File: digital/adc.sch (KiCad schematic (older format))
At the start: 1 part

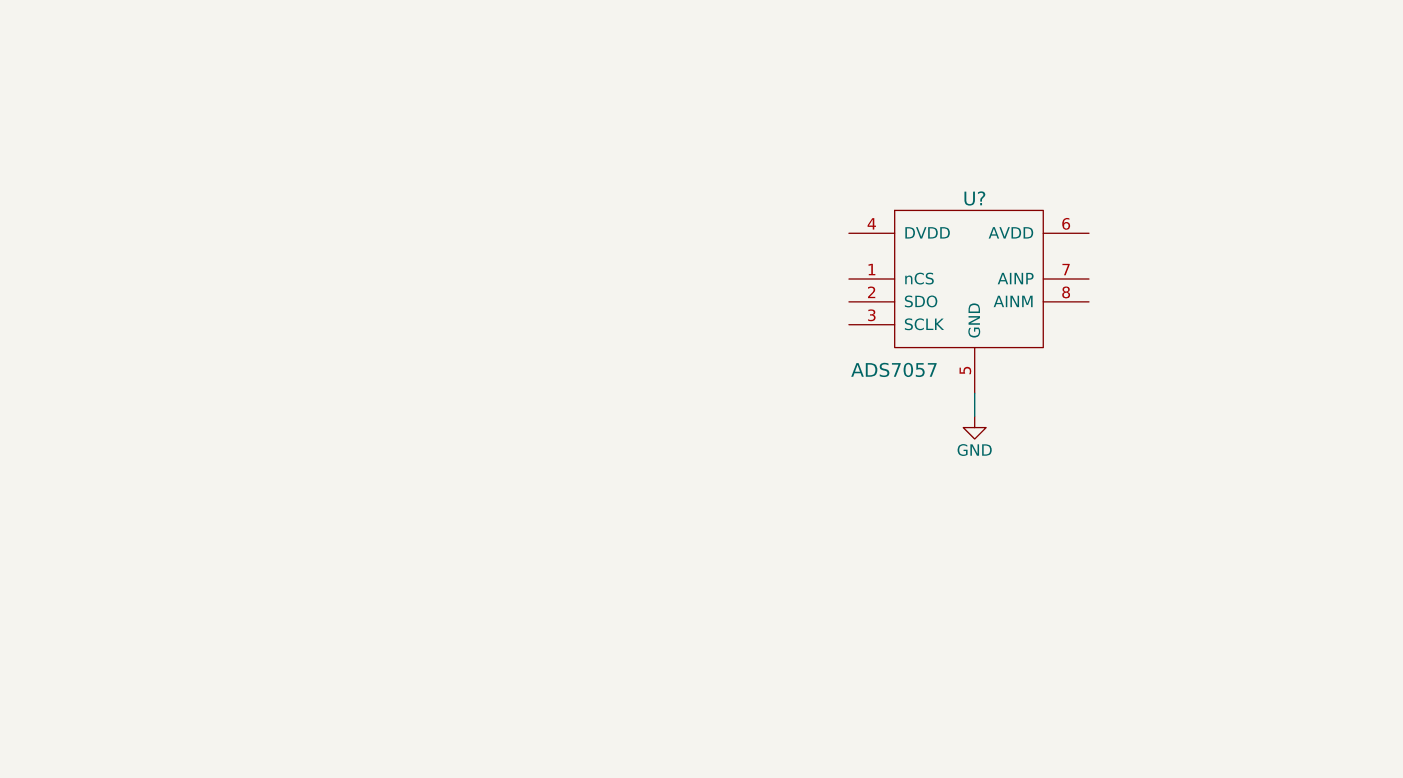
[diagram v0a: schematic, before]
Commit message: Finish schematic TODO footprints
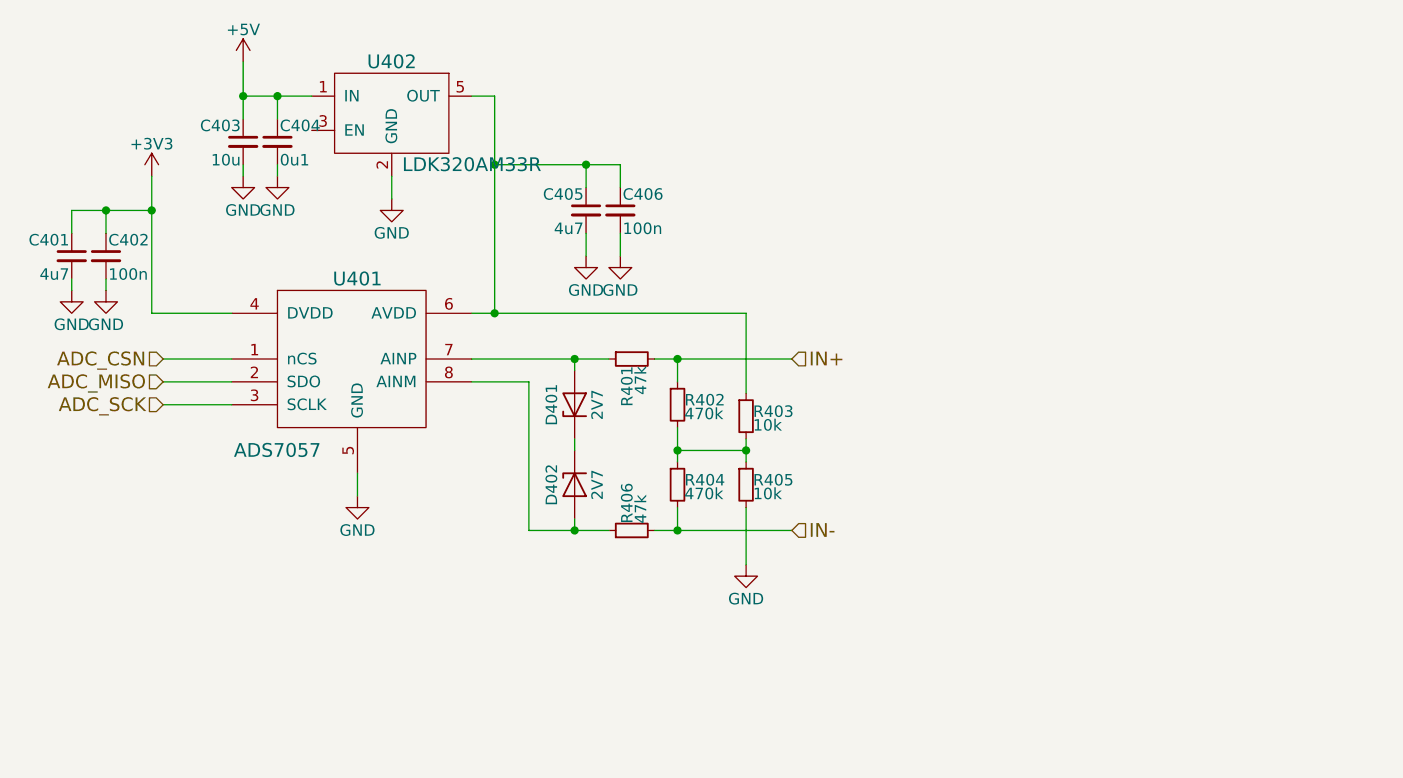
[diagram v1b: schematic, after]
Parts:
- added C401, C405: 4u7, symbol C_Small
- added C402, C406: 100n, symbol C_Small
- added C403: 10u, symbol C_Small
- added C404: 0u1, symbol C_Small
- added D401, D402: 2V7, symbol D_Zener
- added R401, R406: 47k, symbol R_Small
- added R402, R404: 470k, symbol R_Small
- added R403, R405: 10k, symbol R_Small
- added U402: LDK320AM33R, symbol LDK320AM33R
- gave numbers to parts that had none: 1
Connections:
- net GND: now also C401.2, C402.2, C403.2, C404.2, C405.2, C406.2, R405.2, U402.2 (GND)
- net ADC_CSN: now reaches U401.1 (nCS)
- net ADC_MISO: now reaches U401.2 (SDO)
- net ADC_SCK: now reaches U401.3 (SCLK)
- net +3V3: now reaches U401.4 (DVDD)
- net +3V3: now also C401.1, C402.1
- net at U401.6 (AVDD): now also C405.1, C406.1, R403.1, U402.5 (OUT)
- net at U401.7 (AINP): now also D401.2 (A), R401.1
- net at U401.8 (AINM): now also D402.2 (A), R406.1
- new net: D401.1 (K), D402.1 (K)
- new net: R402.2, R403.2, R404.1, R405.1
- new net +5V: C403.1, C404.1, U402.1 (IN)
- new net IN+: R401.2, R402.1
- new net IN-: R404.2, R406.2
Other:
- moved on the sheet: U401

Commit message: Finish schematic and footprinting of digital board
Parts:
- C401, C405: footprint (none) -> Capacitors_SMD:C_1206_HandSoldering
- C402, C404, C406: footprint (none) -> Capacitors_SMD:C_0603_HandSoldering
- C403: footprint (none) -> Capacitors_SMD:C_0805_HandSoldering
- D401, D402: footprint (none) -> Diodes_SMD:D_SOD-323_HandSoldering
- R401, R403, R405, R406: footprint (none) -> Resistors_SMD:R_0603_HandSoldering
- R402, R404: footprint (none) -> Resistors_SMD:R_0402
- U401: footprint (none) -> digital:TI_X2QFN8
- U402: footprint (none) -> digital:ST_SOT23-5L
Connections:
- no-connect marks 0 -> 1
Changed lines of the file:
@@
 F 0 "U401" H 4950 3950 60  0000 C CNN
 F 1 "ADS7057" H 4600 3200 60  0000 C CNN
-F 2 "" H 4950 3650 60  0001 C CNN
+F 2 "digital:TI_X2QFN8" H 4950 3650 60  0001 C CNN
 F 3 "https://www.mouser.com/ProductDetail/Texas-Instruments/ADS7054IRUGR?qs=sGAEpiMZZMvTvDTV69d2QmaaDF3oWAC7QmNCEdeiHEg%3d" H 4950 3650 60  0001 C CNN
 	1    4950 3650
@@
 $EndComp
 $Comp
-L GND #PWR410
+L GND #PWR087
 U 1 1 5AD34755
 P 4950 4300
-F 0 "#PWR410" H 4950 4050 50  0001 C CNN
+F 0 "#PWR087" H 4950 4050 50  0001 C CNN
 F 1 "GND" H 4950 4150 50  0000 C CNN
 F 2 "" H 4950 4300 50  0001 C CNN
@@
 ADC_SCK
 $Comp
-L +3V3 #PWR402
+L +3V3 #PWR088
 U 1 1 5AD705AE
 P 4050 2900
-F 0 "#PWR402" H 4050 2750 50  0001 C CNN
+F 0 "#PWR088" H 4050 2750 50  0001 C CNN
 F 1 "+3V3" H 4050 3040 50  0000 C CNN
 F 2 "" H 4050 2900 50  0001 C CNN
@@
 F 0 "C402" H 3860 3320 50  0000 L CNN
 F 1 "100n" H 3860 3170 50  0000 L CNN
-F 2 "" H 3850 3250 50  0001 C CNN
+F 2 "Capacitors_SMD:C_0603_HandSoldering" H 3850 3250 50  0001 C CNN
 F 3 "" H 3850 3250 50  0001 C CNN
 	1    3850 3250
@@
 F 0 "C401" H 3710 3320 50  0000 L CNN
 F 1 "4u7" H 3710 3170 50  0000 L CNN
-F 2 "" H 3700 3250 50  0001 C CNN
+F 2 "Capacitors_SMD:C_1206_HandSoldering" H 3700 3250 50  0001 C CNN
 F 3 "" H 3700 3250 50  0001 C CNN
 	1    3700 3250
@@
 $EndComp
 $Comp
-L GND #PWR409
+L GND #PWR089
 U 1 1 5AD7062F
 P 3850 3400
-F 0 "#PWR409" H 3850 3150 50  0001 C CNN
+F 0 "#PWR089" H 3850 3150 50  0001 C CNN
 F 1 "GND" H 3850 3250 50  0000 C CNN
 F 2 "" H 3850 3400 50  0001 C CNN
@@
 $EndComp
 $Comp
-L GND #PWR408
+L GND #PWR090
 U 1 1 5AD7064A
 P 3700 3400
-F 0 "#PWR408" H 3700 3150 50  0001 C CNN
+F 0 "#PWR090" H 3700 3150 50  0001 C CNN
 F 1 "GND" H 3700 3250 50  0000 C CNN
 F 2 "" H 3700 3400 50  0001 C CNN
@@
 F 0 "D402" H 5900 4350 50  0000 C CNN
 F 1 "2V7" H 5900 4150 50  0000 C CNN
-F 2 "" H 5900 4250 50  0001 C CNN
+F 2 "Diodes_SMD:D_SOD-323_HandSoldering" H 5900 4250 50  0001 C CNN
 F 3 "https://www.mouser.com/ProductDetail/ON-Semiconductor/MM3Z2V7ST1G?qs=sGAEpiMZZMtQ8nqTKtFS%2fJ7m6e1KBCguKFeJwHBR4ZU%3d" H 5900 4250 50  0001 C CNN
 	1    5900 4250
@@
 F 0 "D401" H 5900 4000 50  0000 C CNN
 F 1 "2V7" H 5900 3800 50  0000 C CNN
-F 2 "" H 5900 3900 50  0001 C CNN
+F 2 "Diodes_SMD:D_SOD-323_HandSoldering" H 5900 3900 50  0001 C CNN
 F 3 "https://www.mouser.com/ProductDetail/ON-Semiconductor/MM3Z2V7ST1G?qs=sGAEpiMZZMtQ8nqTKtFS%2fJ7m6e1KBCguKFeJwHBR4ZU%3d" H 5900 3900 50  0001 C CNN
 	1    5900 3900
@@
 F 0 "R401" H 6180 3720 50  0000 L CNN
 F 1 "47k" H 6180 3660 50  0000 L CNN
-F 2 "" H 6150 3700 50  0001 C CNN
+F 2 "Resistors_SMD:R_0603_HandSoldering" H 6150 3700 50  0001 C CNN
 F 3 "" H 6150 3700 50  0001 C CNN
 	1    6150 3700
@@
 F 0 "R406" H 6180 4470 50  0000 L CNN
 F 1 "47k" H 6180 4410 50  0000 L CNN
-F 2 "" H 6150 4450 50  0001 C CNN
+F 2 "Resistors_SMD:R_0603_HandSoldering" H 6150 4450 50  0001 C CNN
 F 3 "" H 6150 4450 50  0001 C CNN
 	1    6150 4450
@@
 F 0 "R402" H 6380 3920 50  0000 L CNN
 F 1 "470k" H 6380 3860 50  0000 L CNN
-F 2 "" H 6350 3900 50  0001 C CNN
+F 2 "Resistors_SMD:R_0402" H 6350 3900 50  0001 C CNN
 F 3 "" H 6350 3900 50  0001 C CNN
 	1    6350 3900
@@
 F 0 "R404" H 6380 4270 50  0000 L CNN
 F 1 "470k" H 6380 4210 50  0000 L CNN
-F 2 "" H 6350 4250 50  0001 C CNN
+F 2 "Resistors_SMD:R_0402" H 6350 4250 50  0001 C CNN
 F 3 "" H 6350 4250 50  0001 C CNN
 	1    6350 4250
@@
 F 0 "R403" H 6680 3970 50  0000 L CNN
 F 1 "10k" H 6680 3910 50  0000 L CNN
-F 2 "" H 6650 3950 50  0001 C CNN
+F 2 "Resistors_SMD:R_0603_HandSoldering" H 6650 3950 50  0001 C CNN
 F 3 "" H 6650 3950 50  0001 C CNN
 	1    6650 3950
@@
 F 0 "R405" H 6680 4270 50  0000 L CNN
 F 1 "10k" H 6680 4210 50  0000 L CNN
-F 2 "" H 6650 4250 50  0001 C CNN
+F 2 "Resistors_SMD:R_0603_HandSoldering" H 6650 4250 50  0001 C CNN
 F 3 "" H 6650 4250 50  0001 C CNN
 	1    6650 4250
@@
 Connection ~ 6350 4100
 $Comp
-L GND #PWR411
+L GND #PWR091
 U 1 1 5AD86212
 P 6650 4600
-F 0 "#PWR411" H 6650 4350 50  0001 C CNN
+F 0 "#PWR091" H 6650 4350 50  0001 C CNN
 F 1 "GND" H 6650 4450 50  0000 C CNN
 F 2 "" H 6650 4600 50  0001 C CNN
@@
 F 0 "C406" H 6110 3120 50  0000 L CNN
 F 1 "100n" H 6110 2970 50  0000 L CNN
-F 2 "" H 6100 3050 50  0001 C CNN
+F 2 "Capacitors_SMD:C_0603_HandSoldering" H 6100 3050 50  0001 C CNN
 F 3 "" H 6100 3050 50  0001 C CNN
 	1    6100 3050
@@
 F 0 "C405" H 5960 3120 50  0000 L CNN
 F 1 "4u7" H 5960 2970 50  0000 L CNN
-F 2 "" H 5950 3050 50  0001 C CNN
+F 2 "Capacitors_SMD:C_1206_HandSoldering" H 5950 3050 50  0001 C CNN
 F 3 "" H 5950 3050 50  0001 C CNN
 	1    5950 3050
@@
 $EndComp
 $Comp
-L GND #PWR406
+L GND #PWR092
 U 1 1 5AD86984
 P 5950 3250
-F 0 "#PWR406" H 5950 3000 50  0001 C CNN
+F 0 "#PWR092" H 5950 3000 50  0001 C CNN
 F 1 "GND" H 5950 3100 50  0000 C CNN
 F 2 "" H 5950 3250 50  0001 C CNN
@@
 $EndComp
 $Comp
-L GND #PWR407
+L GND #PWR093
 U 1 1 5AD869BD
 P 6100 3250
-F 0 "#PWR407" H 6100 3000 50  0001 C CNN
+F 0 "#PWR093" H 6100 3000 50  0001 C CNN
 F 1 "GND" H 6100 3100 50  0000 C CNN
 F 2 "" H 6100 3250 50  0001 C CNN
@@
 U 1 1 5ADA8C95
 P 5100 2550
+AR Path="/5ADA8C95" Ref="U402"  Part="1"
+AR Path="/5AD346DB/5ADA8C95" Ref="U402"  Part="1"
 F 0 "U402" H 5100 2700 60  0000 C CNN
 F 1 "LDK320AM33R" H 5450 2250 60  0000 C CNN
-F 2 "" H 5100 2550 60  0001 C CNN
+F 2 "digital:ST_SOT23-5L" H 5100 2550 60  0001 C CNN
 F 3 "https://www.mouser.com/ProductDetail/STMicroelectronics/LDK320AM33R?qs=sGAEpiMZZMsGz1a6aV8DcGP3s75Ab7uy0gVNUtcA%252bWU%3d" H 5100 2550 60  0001 C CNN
 	1    5100 2550
@@
 Connection ~ 5550 2850
 $Comp
-L +5V #PWR401
+L +5V #PWR094
 U 1 1 5ADA8E18
 P 4450 2400
-F 0 "#PWR401" H 4450 2250 50  0001 C CNN
+F 0 "#PWR094" H 4450 2250 50  0001 C CNN
 F 1 "+5V" H 4450 2540 50  0000 C CNN
 F 2 "" H 4450 2400 50  0001 C CNN
@@
 F 0 "C404" H 4610 2820 50  0000 L CNN
 F 1 "0u1" H 4610 2670 50  0000 L CNN
-F 2 "" H 4600 2750 50  0001 C CNN
+F 2 "Capacitors_SMD:C_0603_HandSoldering" H 4600 2750 50  0001 C CNN
 F 3 "" H 4600 2750 50  0001 C CNN
 	1    4600 2750
@@
 F 0 "C403" H 4460 2820 50  0000 L CNN
 F 1 "10u" H 4460 2670 50  0000 L CNN
-F 2 "" H 4450 2750 50  0001 C CNN
+F 2 "Capacitors_SMD:C_0805_HandSoldering" H 4450 2750 50  0001 C CNN
 F 3 "" H 4450 2750 50  0001 C CNN
 	1    4450 2750
@@
 $EndComp
 $Comp
-L GND #PWR403
+L GND #PWR095
 U 1 1 5ADA8EE6
 P 4450 2900
-F 0 "#PWR403" H 4450 2650 50  0001 C CNN
+F 0 "#PWR095" H 4450 2650 50  0001 C CNN
 F 1 "GND" H 4450 2750 50  0000 C CNN
 F 2 "" H 4450 2900 50  0001 C CNN
@@
 	4450 2850 4450 2900
 $Comp
-L GND #PWR404
+L GND #PWR096
 U 1 1 5ADA8FD8
 P 4600 2900
-F 0 "#PWR404" H 4600 2650 50  0001 C CNN
+F 0 "#PWR096" H 4600 2650 50  0001 C CNN
 F 1 "GND" H 4600 2750 50  0000 C CNN
 F 2 "" H 4600 2900 50  0001 C CNN
@@
 Connection ~ 4600 2550
 $Comp
-L GND #PWR405
+L GND #PWR097
 U 1 1 5ADA9622
 P 5100 3000
-F 0 "#PWR405" H 5100 2750 50  0001 C CNN
+F 0 "#PWR097" H 5100 2750 50  0001 C CNN
 F 1 "GND" H 5100 2850 50  0000 C CNN
 F 2 "" H 5100 3000 50  0001 C CNN
@@
 Wire Wire Line
 	5100 2900 5100 3000
+NoConn ~ 4750 2700
 $EndSCHEMATC

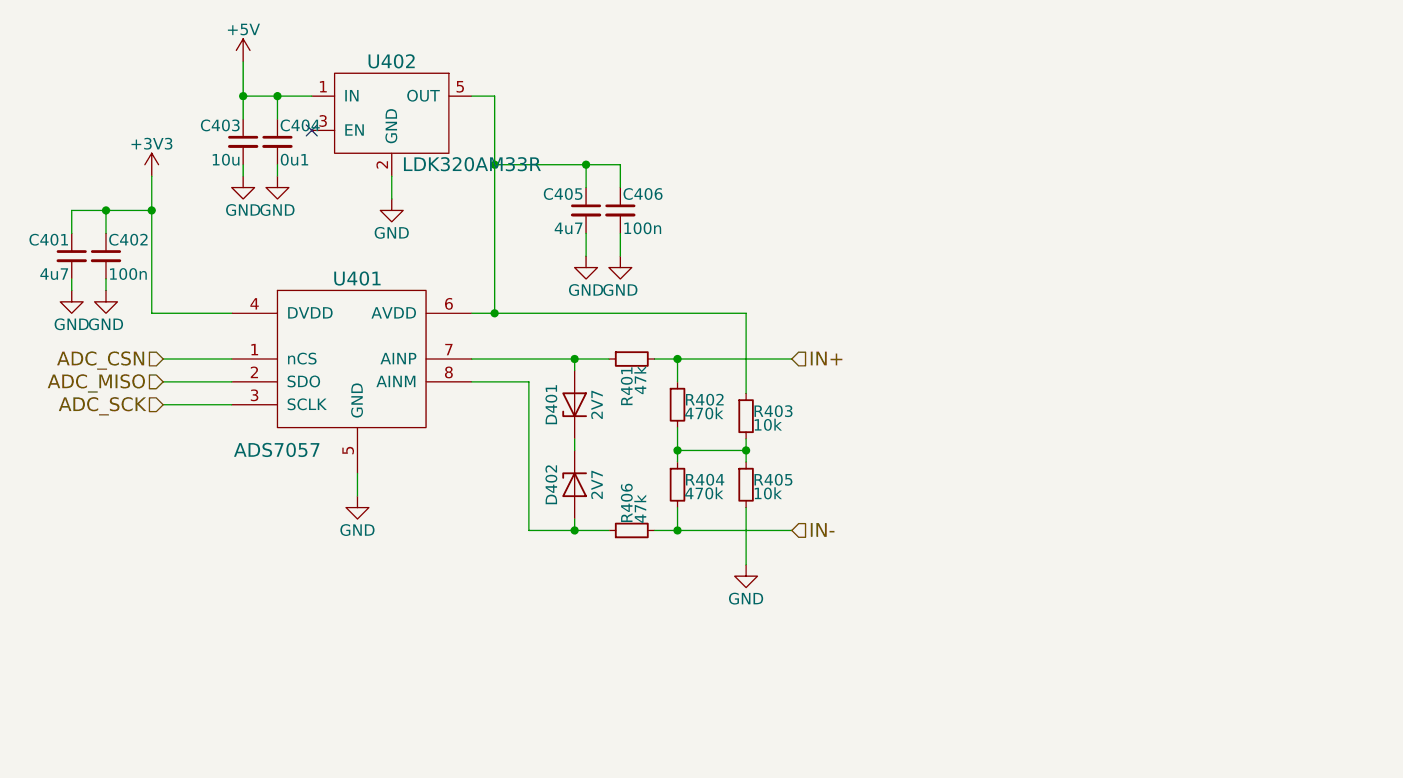
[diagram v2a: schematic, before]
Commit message: Add gain stage; hopefully ready to start layout now
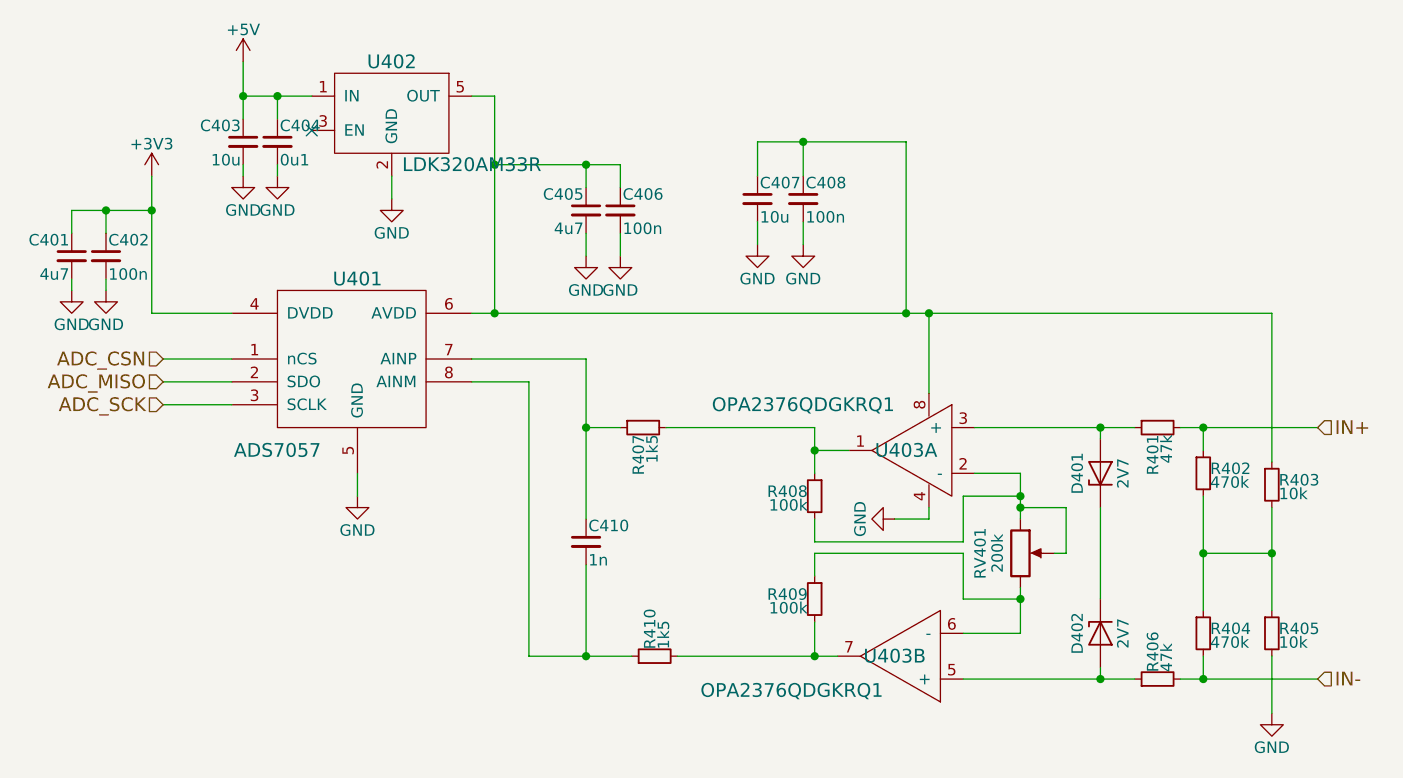
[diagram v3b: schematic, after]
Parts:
- added C407: 10u, Capacitors_SMD:C_0805_HandSoldering, symbol C_Small
- added C408: 100n, Capacitors_SMD:C_0603_HandSoldering, symbol C_Small
- added C410: 1n, Capacitors_SMD:C_0603_HandSoldering, symbol C_Small
- added R407, R410: 1k5, Resistors_SMD:R_0402, symbol R_Small
- added R408, R409: 100k, Resistors_SMD:R_0402, symbol R_Small
- added RV401: 200k, digital:PT10LV10-204A2020, symbol POT
- added U403: OPA2376QDGKRQ1, digital:TI_VSSOP8, symbol OPA2376QDGKRQ1
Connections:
- net GND: now also C407.2, C408.2, U403.4
- net at C405.1, C406.1, R403.1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: now also C407.1, C408.1, U403.8
- net at D401.2 (A), R401.1: now also U403.3 (+); no longer U401.7 (AINP)
- net at D402.2 (A), R406.1: now also U403.5 (+); no longer U401.8 (AINM)
- new net: C410.1, R407.1, U401.7 (AINP)
- new net: C410.2, R410.1, U401.8 (AINM)
- new net: R407.2, R408.1, U403.1
- new net: R408.2, RV401.1, RV401.2, U403.2 (-)
- new net: R409.1, RV401.3, U403.6 (-)
- new net: R409.2, R410.2, U403.7
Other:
- moved on the sheet: D401, D402, R401, R402, R403, R404, R405, R406
